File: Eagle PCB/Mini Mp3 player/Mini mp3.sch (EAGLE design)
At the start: 16 parts, among them U2 ATMEGA328P-PU

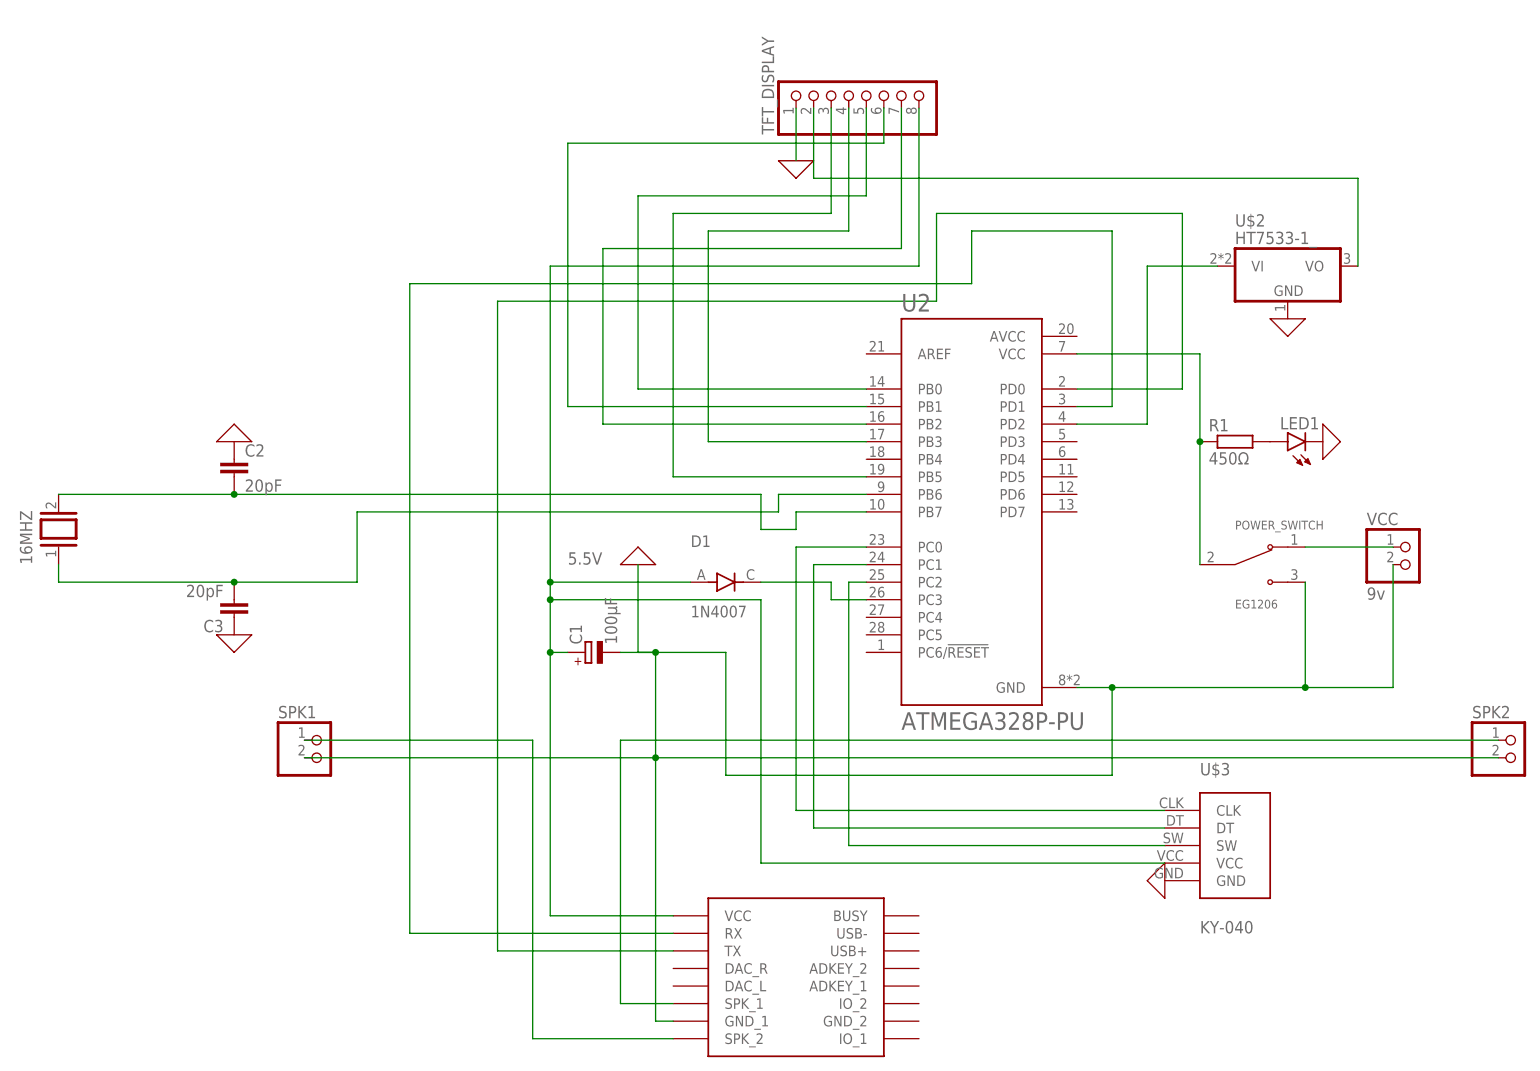
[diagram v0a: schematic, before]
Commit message: Voltage divider included and updated Mini display
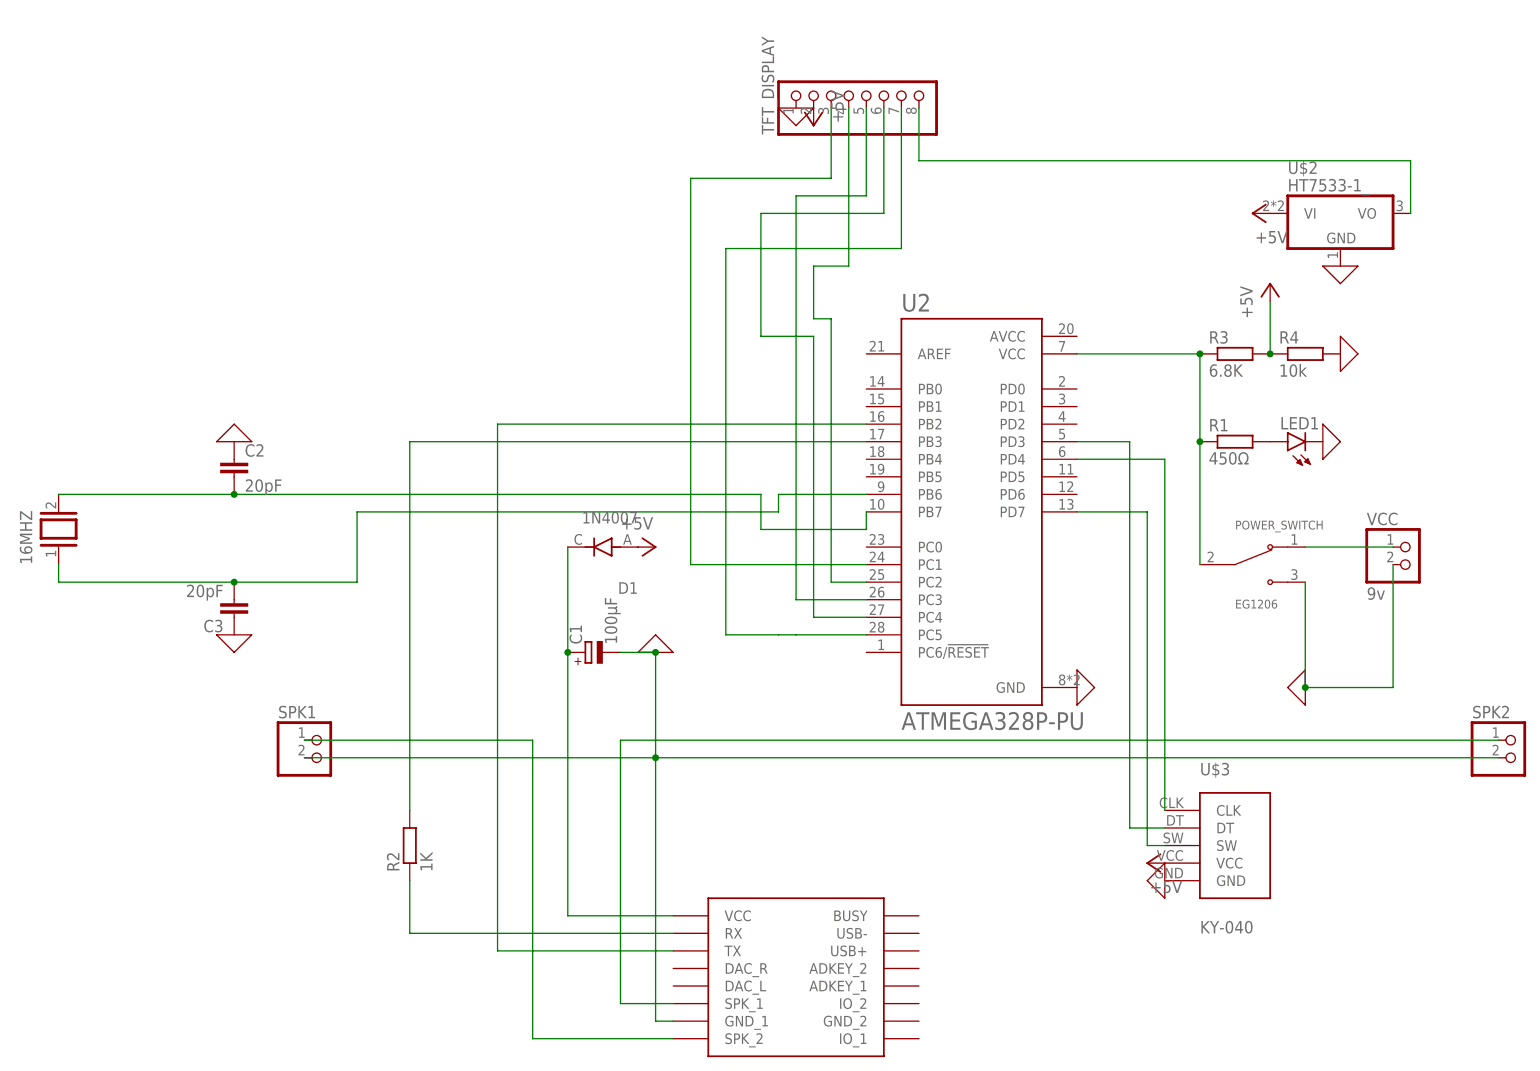
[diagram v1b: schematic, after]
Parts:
- added R2: 1K, rcl:R-EU_0204/7
- added R3: 6.8K, rcl:R-EU_0204/7
- added R4: 10k, rcl:R-EU_0204/7
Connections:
- removed net 5.5V: C1.+, D1.A, TFT_DISPLAY.8, U$1.VCC, U$3.VCC
- new net +5V: D1.A, R3.2, R4.1, TFT_DISPLAY.2, U$2.VI, U$3.VCC
- new net N$20: U$3.CLK, U2.PD4
- net 0: now also R4.2; no longer C1.-, SPK1.2, SPK2.2, U$1.GND_1
- net N$1: now also R2.2, U2.PB3; no longer U$1.RX, U2.PD1
- net N$10: now also C1.-, SPK1.2, SPK2.2, U$1.GND_1; no longer TFT_DISPLAY.7, U2.PB2
- net N$11: now also C1.+, D1.C, U$1.VCC; no longer TFT_DISPLAY.6, U2.PB1
- net N$12: now also R3.1
- net N$14: now also R2.1, U$1.RX; no longer U$3.DT, U2.PC1
- net N$15: now also U$3.SW, U2.PD7; no longer D1.C, U2.PC3
- net N$16: now also U$3.DT, U2.PD3; no longer U$3.SW, U2.PC2
- net N$2: now also U2.PB2; no longer U2.PD0
- net N$3: now also TFT_DISPLAY.6, U2.PC4; no longer U$3.CLK, U2.PC0
- net N$5: now also TFT_DISPLAY.8; no longer TFT_DISPLAY.2
- net N$6: now also TFT_DISPLAY.7, U2.PC5; no longer U$2.VI, U2.PD2
- net N$7: now also TFT_DISPLAY.5, U2.PC3; no longer TFT_DISPLAY.3, U2.PB5
- net N$8: now also U2.PC2; no longer U2.PB3
- net N$9: now also TFT_DISPLAY.3, U2.PC1; no longer TFT_DISPLAY.5, U2.PB0
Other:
- moved on the sheet: D1, U$2
